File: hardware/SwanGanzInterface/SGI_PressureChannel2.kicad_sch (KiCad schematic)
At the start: 0 parts

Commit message: Developed amplifier circuits
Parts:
- added C14: 0.1u, Capacitor_SMD:C_0603_1608Metric, symbol Device:C
- added C15, C16: C, symbol Device:C
- added R15, R16, R17: R, symbol Device:R
- added R18, R19: 0R, symbol Device:R
- added U5: OPA2350, Package_DIP:DIP-8_W7.62mm, symbol SGI_SymbolLib:OPA2350PA
- added U6: INA122D, Package_SO:SOIC-8_5.3x5.3mm_P1.27mm, symbol SGI_SymbolLib:INA122D
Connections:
- new net: C16.1, R17.2, U5.5 (+)
- new net: R18.2, R19.1, U5.6 (-)
- new net: R16.1, U6.6 (OUT)
- new net: C15.1, R16.2, R17.1
- new net: R15.1, U6.1 (RG+)
- new net: R15.2, U6.8 (RG-)
- new net +3V3A: C14.2, U6.7 (+VS)
- new net AGND: C14.1, C15.2, R18.1, U6.4 (-VS), U6.5 (REF)
- new net Pres2AmpOut: C16.2, R19.2, U5.7

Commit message: Filter Parameters
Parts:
- C15, C16: value C -> 0.1u
- R16, R17: value R -> 32k
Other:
- note added: "50 Hz Cutoff"
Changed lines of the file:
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@@
 	(generator "eeschema")
 	(generator_version "9.0")
-	(paper "A3")
+	(paper "A4")
 	(title_block
 		(title "Swan Ganz Interface")
-		(date "2025-12-20")
+		(date "2026-01-12")
 		(rev "Rev 1.0")
 		(company "Univerisity of Texas at Austin")
@@
 		(comment 2 "Ashton Knecht, Jack Son, Nathan DeLaRosa, Jerry Xia")
 		(comment 3 "Faculty Mentor - Dr. Valvano")
+	)
+	(text "50 Hz Cutoff"
+		(exclude_from_sim no)
+		(at 117.475 24.13 0)
+		(effects
+			(font
+				(size 1.27 1.27)
+			)
+		)
 	)
 	(junction
@@
 			)
 		)
-		(property "Value" "R"
+		(property "Value" "32k"
 			(at 118.745 61.595 90)
 			(effects
@@
 			)
 		)
-		(property "Value" "R"
+		(property "Value" "32k"
 			(at 132.715 61.595 90)
 			(effects
@@
 			)
 		)
-		(property "Value" "C"
-			(at 152.4 56.515 90)
+		(property "Value" "0.1u"
+			(at 153.67 56.515 90)
 			(effects
 				(font
@@
 			)
 		)
-		(property "Value" "C"
+		(property "Value" "0.1u"
 			(at 126.365 71.12 0)
 			(effects

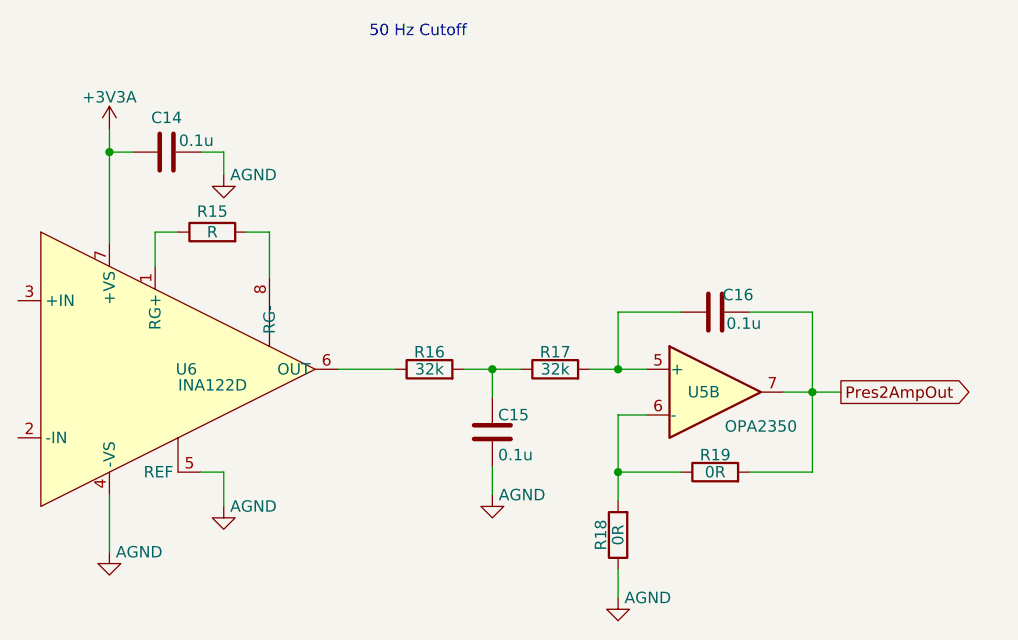
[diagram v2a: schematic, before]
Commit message: Finished MSP-LP Symbol, Started Pressure_Connector Symbol
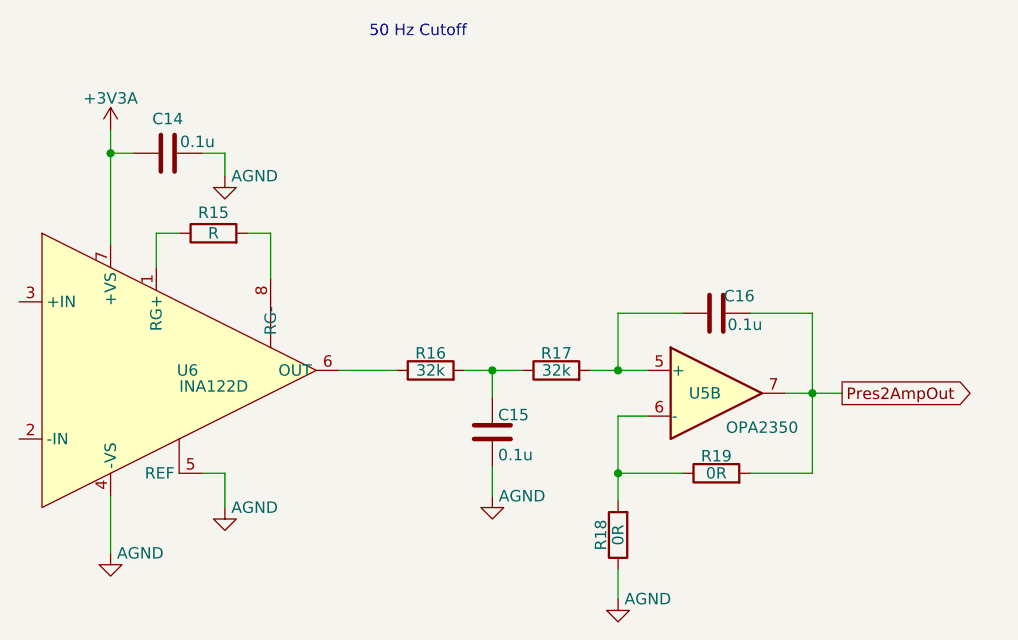
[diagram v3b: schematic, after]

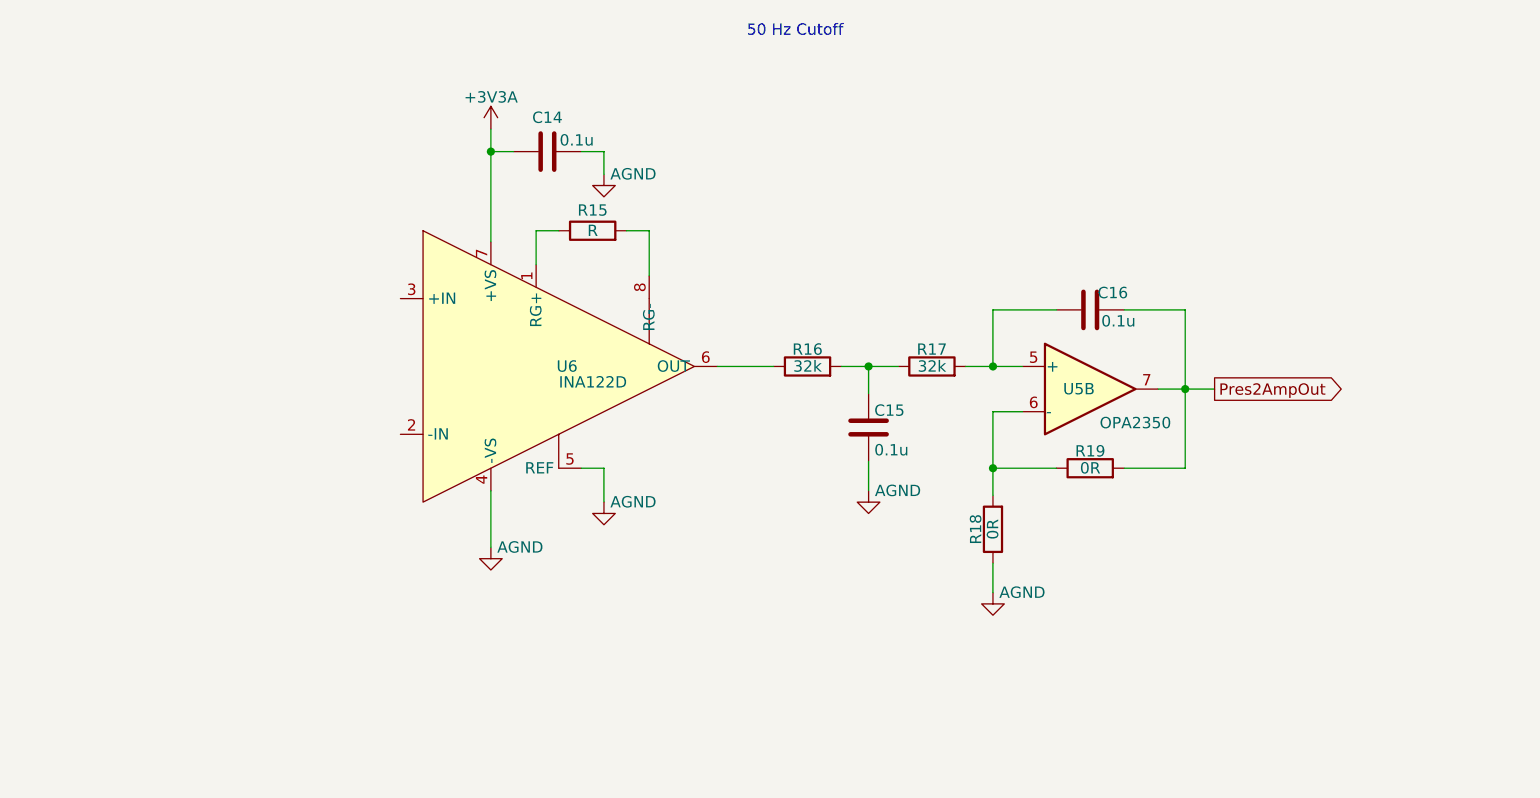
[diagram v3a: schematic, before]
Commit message: Updated gain and added power connector
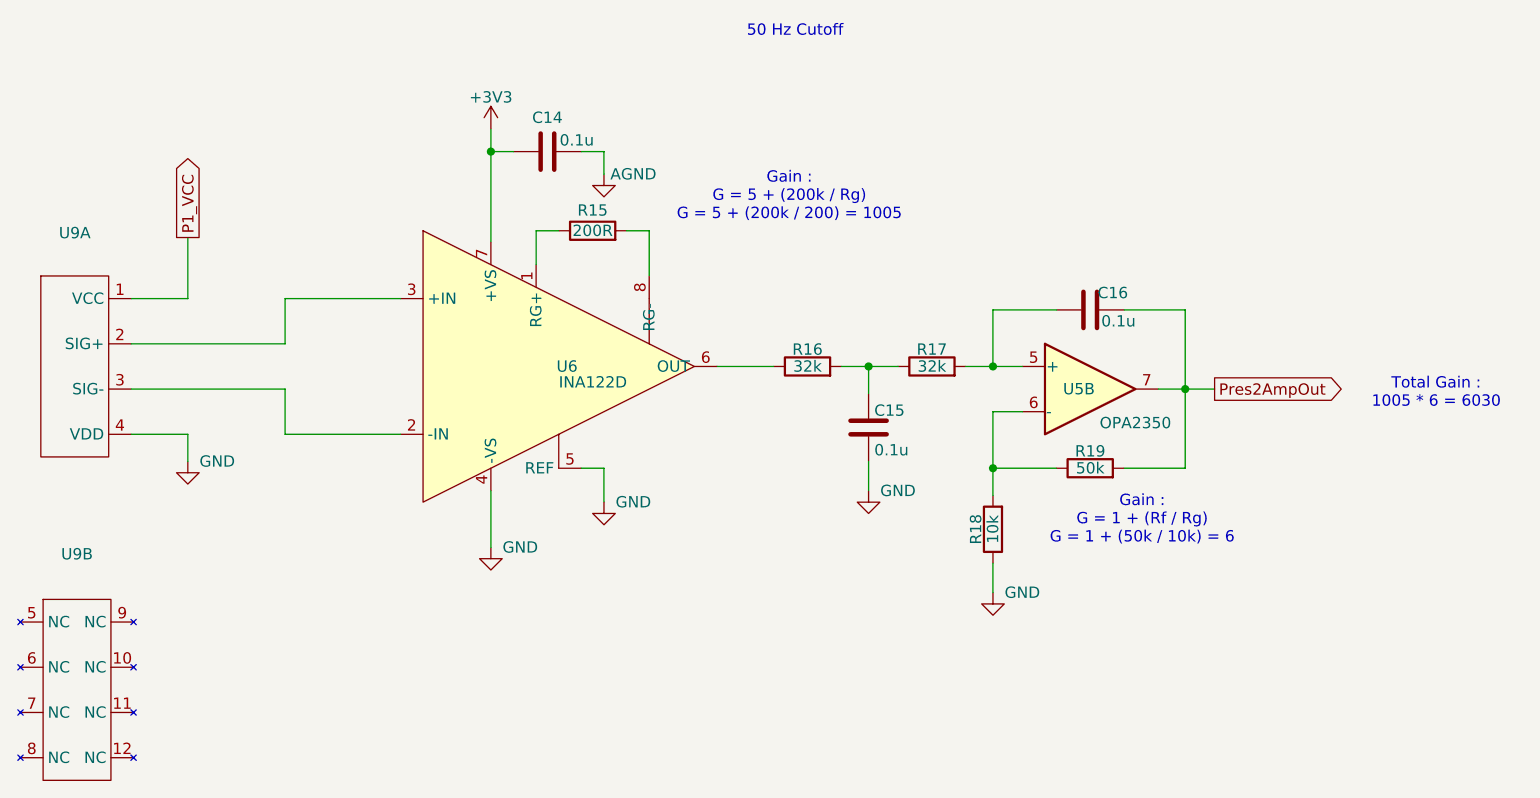
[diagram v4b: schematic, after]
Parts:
- added U9: ~, symbol SGI_SymbolLib:Pressure_Connector
- R15: value R -> 200R
- R18: value 0R -> 10k
- R19: value 0R -> 50k
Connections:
- net AGND: no longer C15.2, R18.1, U6.4 (-VS), U6.5 (REF)
- net at U6.2 (-IN): now also U9.3 (SIG-)
- net at U6.3 (+IN): now also U9.2 (SIG+)
- net +3V3A renamed +3V3
- new net GND: C15.2, R18.1, U6.4 (-VS), U6.5 (REF), U9.4 (VDD)
- new net P1_VCC: U9.1 (VCC)
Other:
- note added: "Gain : G = 1 + (Rf / Rg) G = 1 + (50k / 10k) = 6"
- note added: "Gain : G = 5 + (200k / Rg) G = 5 + (200k / 200) = 1005"
- note added: "Total Gain : 1005 * 6 = 6030"

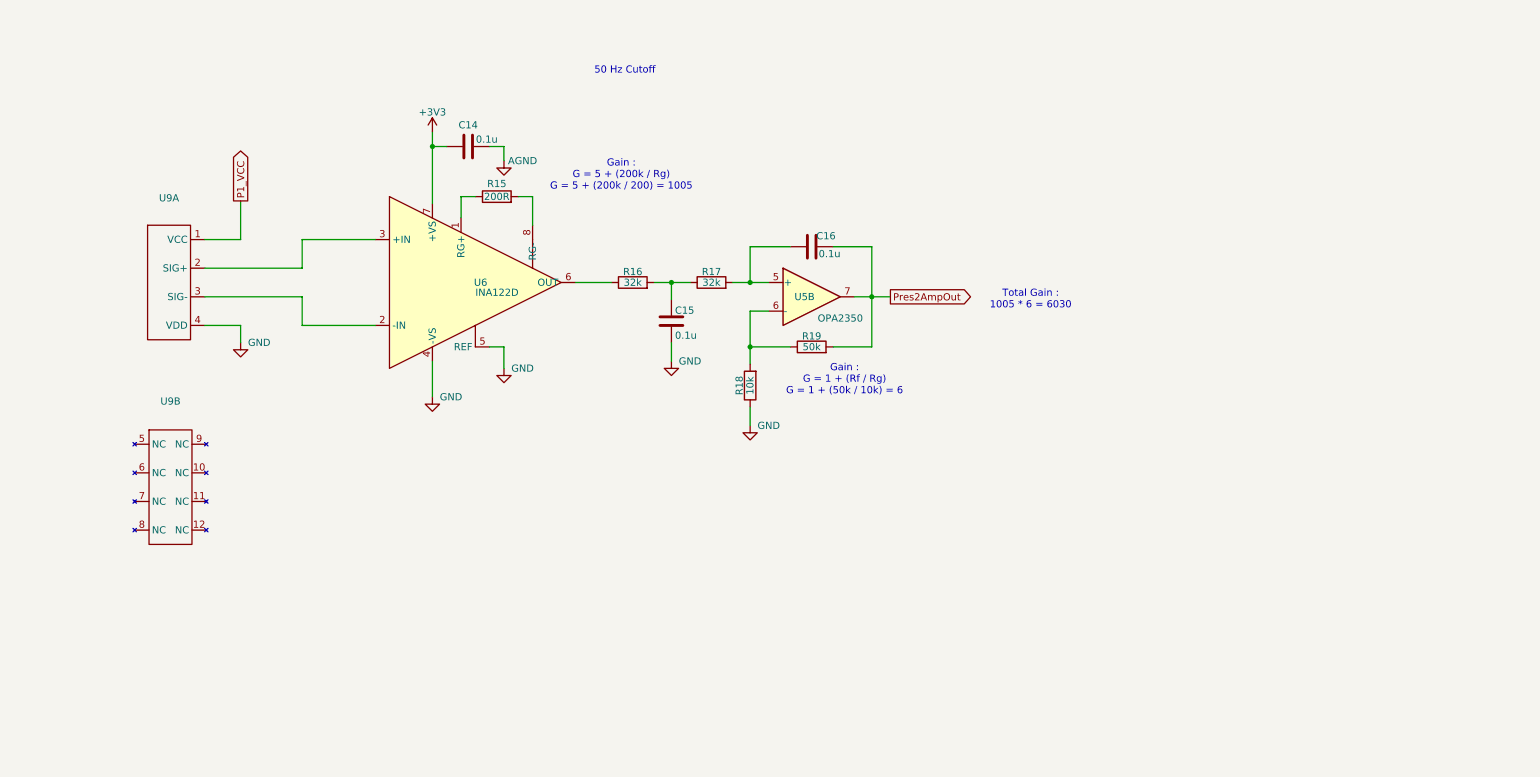
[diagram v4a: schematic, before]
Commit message: Reverse Polarity Fet, Updated Notes, Added second gain stage for pressure, General Updates
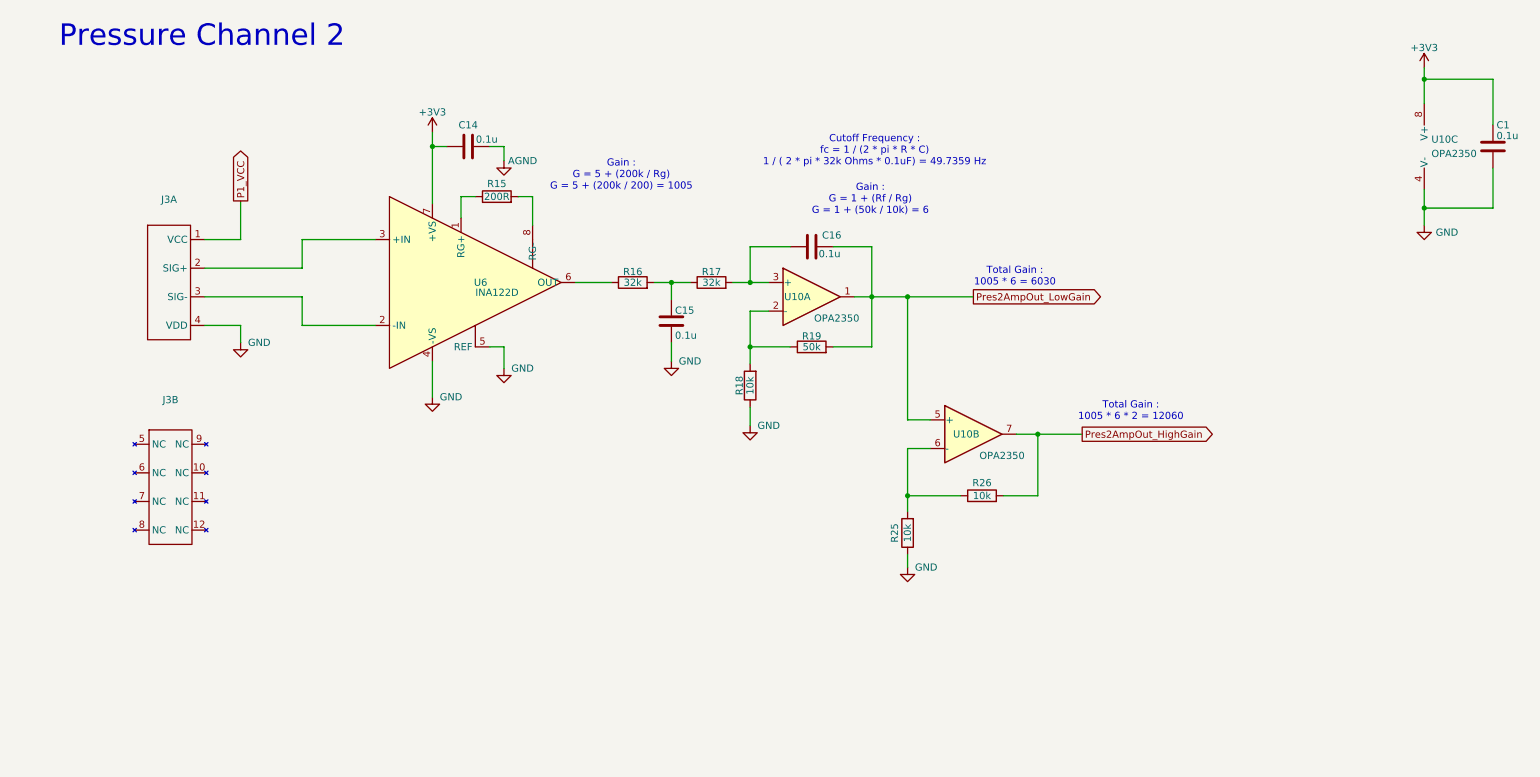
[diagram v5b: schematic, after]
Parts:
- removed U5: OPA2350, Package_DIP:DIP-8_W7.62mm, symbol SGI_SymbolLib:OPA2350PA
- added C1: 0.1u, symbol Device:C
- added R25, R26: 10k, symbol Device:R
- added U10: OPA2350, Package_DIP:DIP-8_W7.62mm, symbol SGI_SymbolLib:OPA2350PA
- renumbered U9 to J3
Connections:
- net +3V3: now also C1.1, U10.8 (V+)
- net GND: now also C1.2, R25.1, U10.4 (V-)
- net at C16.1, R17.2: now also U10.3 (+)
- net at R18.2, R19.1: now also U10.2 (-)
- net Pres2AmpOut renamed Pres2AmpOut_LowGain
- net Pres2AmpOut_LowGain: now also U10.1, U10.5 (+)
- new net: R25.2, R26.1, U10.6 (-)
- new net Pres2AmpOut_HighGain: R26.2, U10.7
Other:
- note added: "Cutoff Frequency : fc = 1 / (2 * pi * R * C) 1 / ( 2 * pi * 32k Ohms * 0.1uF) = 49.7359 Hz"
- note added: "Pressure Channel 2"
- note added: "Total Gain : 1005 * 6 * 2 = 12060"
- note removed: "50 Hz Cutoff"

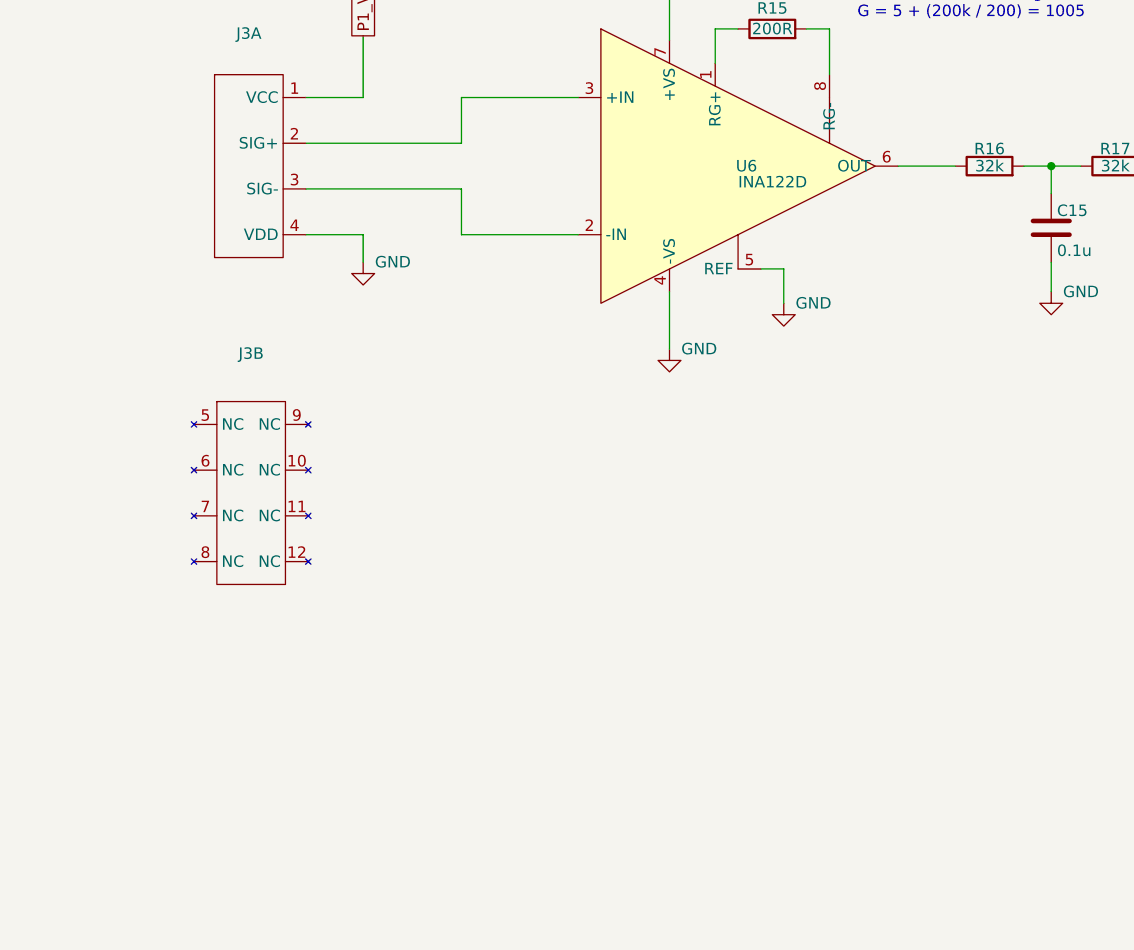
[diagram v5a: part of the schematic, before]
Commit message: Added launchpad, power jumpers, messed with symbol lib
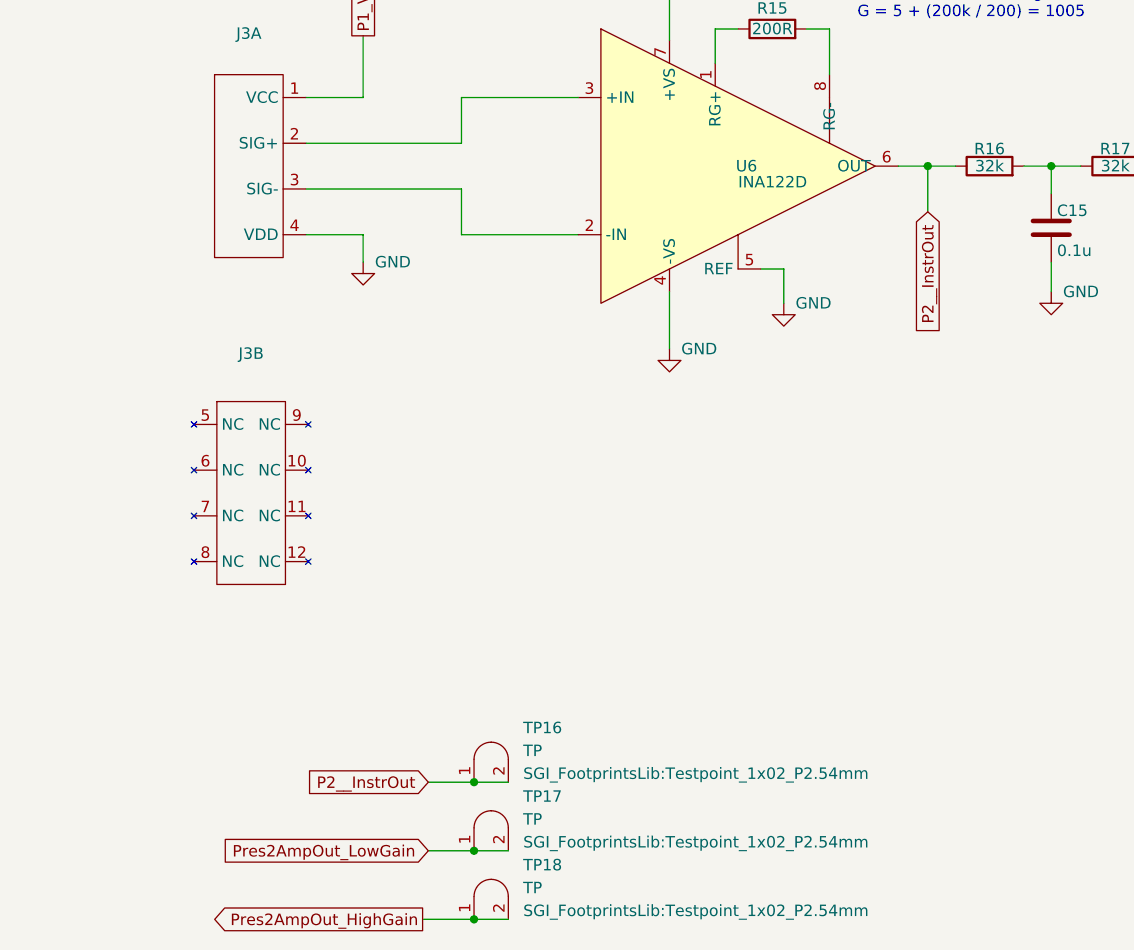
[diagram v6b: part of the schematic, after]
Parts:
- added TP16, TP17, TP18: TP, SGI_FootprintsLib:Testpoint_1x02_P2.54mm, symbol SGI_SymbolLib:Testpoint
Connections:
- net Pres2AmpOut_HighGain: now also TP18.1 (A), TP18.2 (B)
- net Pres2AmpOut_LowGain: now also TP17.1 (A), TP17.2 (B)
- net P2__InstrOut: now reaches R16.1, U6.6 (OUT)
- net P2__InstrOut: now also TP16.1 (A), TP16.2 (B)
